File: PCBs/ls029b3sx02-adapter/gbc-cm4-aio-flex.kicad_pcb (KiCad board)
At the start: 2 copper layers, 34.4 x 31.4 mm, 15 parts, among them J2 WP7B-S040VA1-R6000, J3 Conn_01x40, K1 TestPoint, Q1 BC847

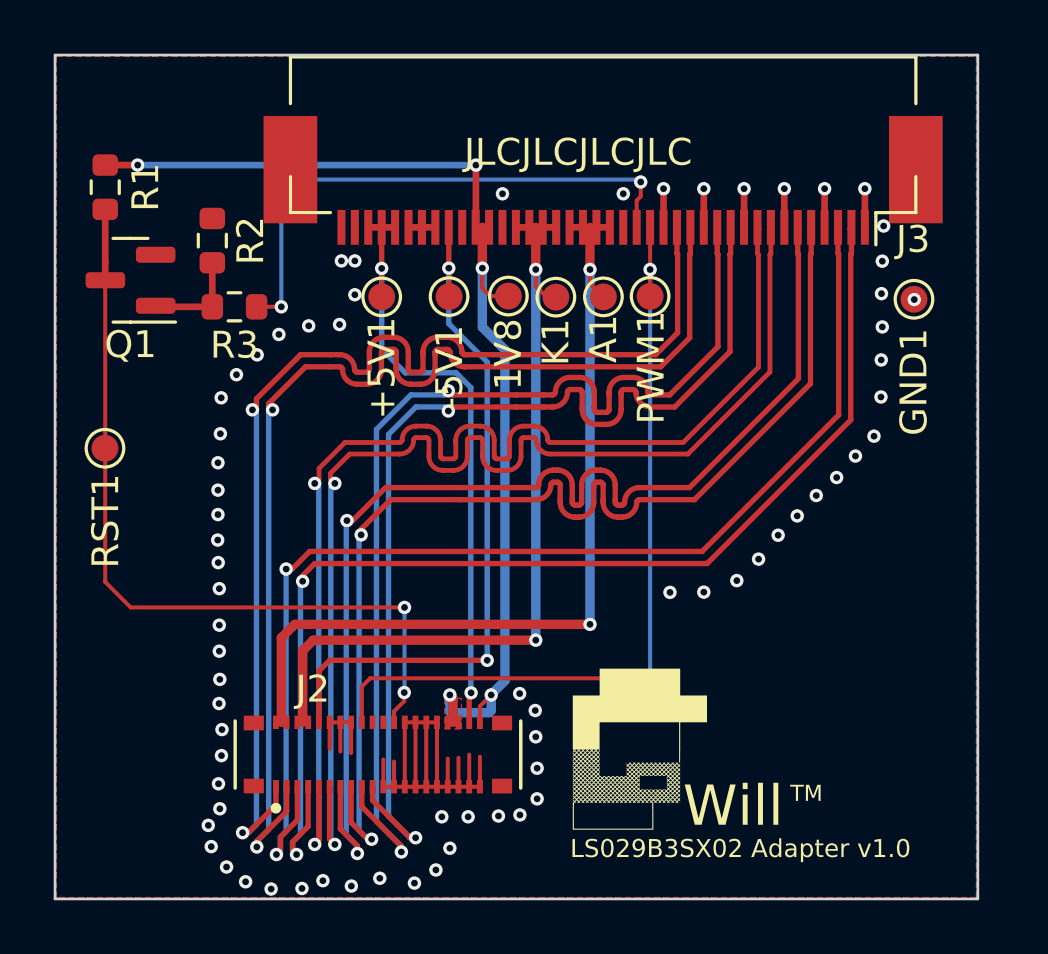
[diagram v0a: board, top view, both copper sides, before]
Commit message: fix ls029b3sx02-adapter connector package
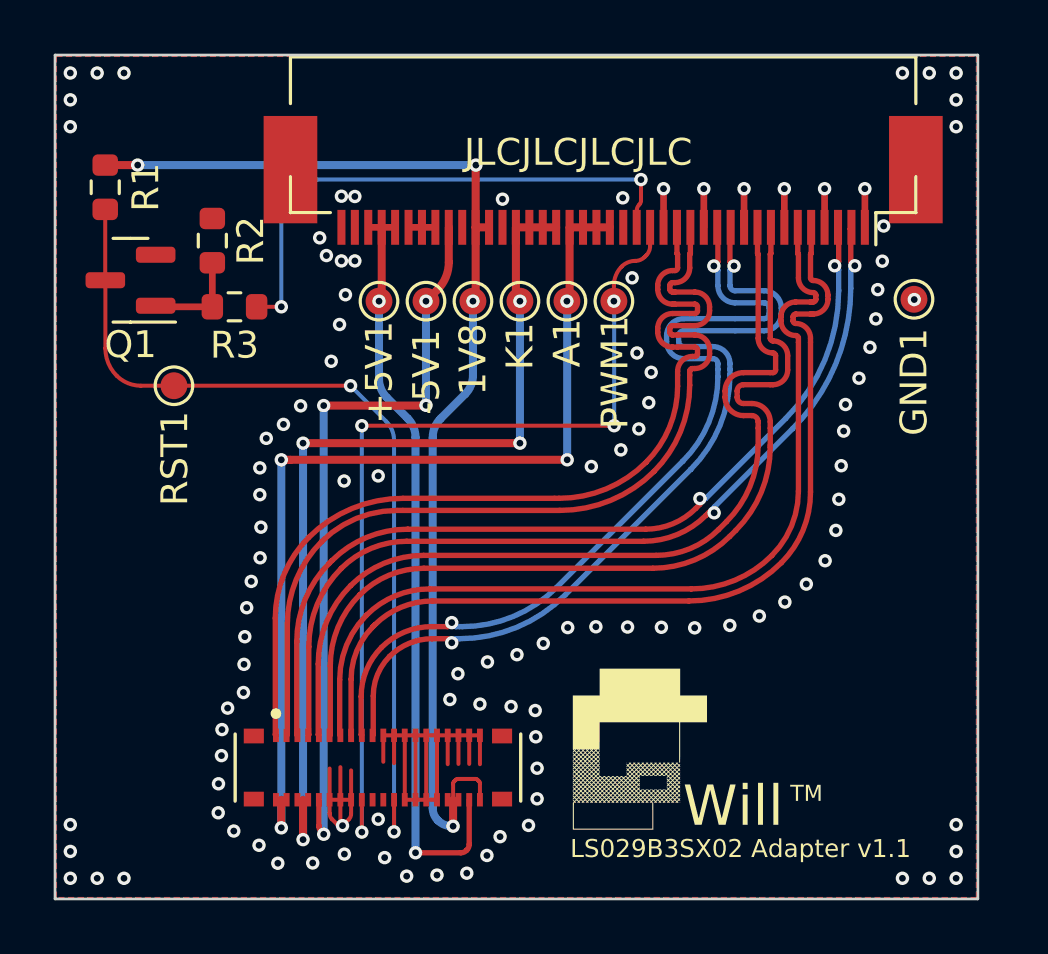
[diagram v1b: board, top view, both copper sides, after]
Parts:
- moved RST1 3.47 mm to (140.4, 126.2)
- moved A1 1.37 mm to (155.0, 123.0)
- moved PWM1 1.36 mm to (156.8, 123.0)
- moved K1 1.35 mm to (153.2, 123.0)
- moved 1V8 1.33 mm to (151.5, 123.0)
- moved -5V1 0.88 mm to (149.8, 123.0)
- moved J2 0.49 mm to (148.0, 140.4), turned to 180 degrees
- moved +5V1 0.19 mm to (148.0, 123.0)
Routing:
- net /D0_N: track 43.6 -> 33.1 mm
- net /D0_P: track 43.6 -> 33.2 mm
- net /D3_P: track 44.1 -> 34.5 mm, vias 2 -> 0
- net /CLK_P: track 44.1 -> 34.4 mm, vias 2 -> 0
- net /CLK_N: track 44.0 -> 34.5 mm, vias 2 -> 0
- net /D1_N: track 43.7 -> 34.6 mm, vias 2 -> 0
- net /D3_N: track 43.3 -> 34.5 mm, vias 2 -> 0
- net /D1_P: track 42.8 -> 34.5 mm, vias 2 -> 0
- net /D2_N: track 40.5 -> 33.0 mm
- net /D2_P: track 39.7 -> 33.0 mm
- net +5V: track 23.0 -> 28.7 mm
- net /PWM: track 30.0 -> 33.9 mm, vias 2 -> 4
- net /LCD_K: track 30.3 -> 33.9 mm, vias 2 -> 4
- net GND: track 33.5 -> 36.9 mm, vias 70 -> 110
- net /RESET: track 30.5 -> 33.5 mm
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- removed copper zone on F.Cu, net /LCD_K
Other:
- board text added: "LS029B3SX02 Adapter v1.1"
- board text removed: "LS029B3SX02 Adapter v1.0"
